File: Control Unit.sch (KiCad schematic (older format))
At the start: 54 parts, among them SW1 SW_Push-Switch, U19 7400, U20 74LS161-74xx, U21 AT28C64B-15PU, U22 AT28C64B-15PU, U23 AT28C64B-15PU

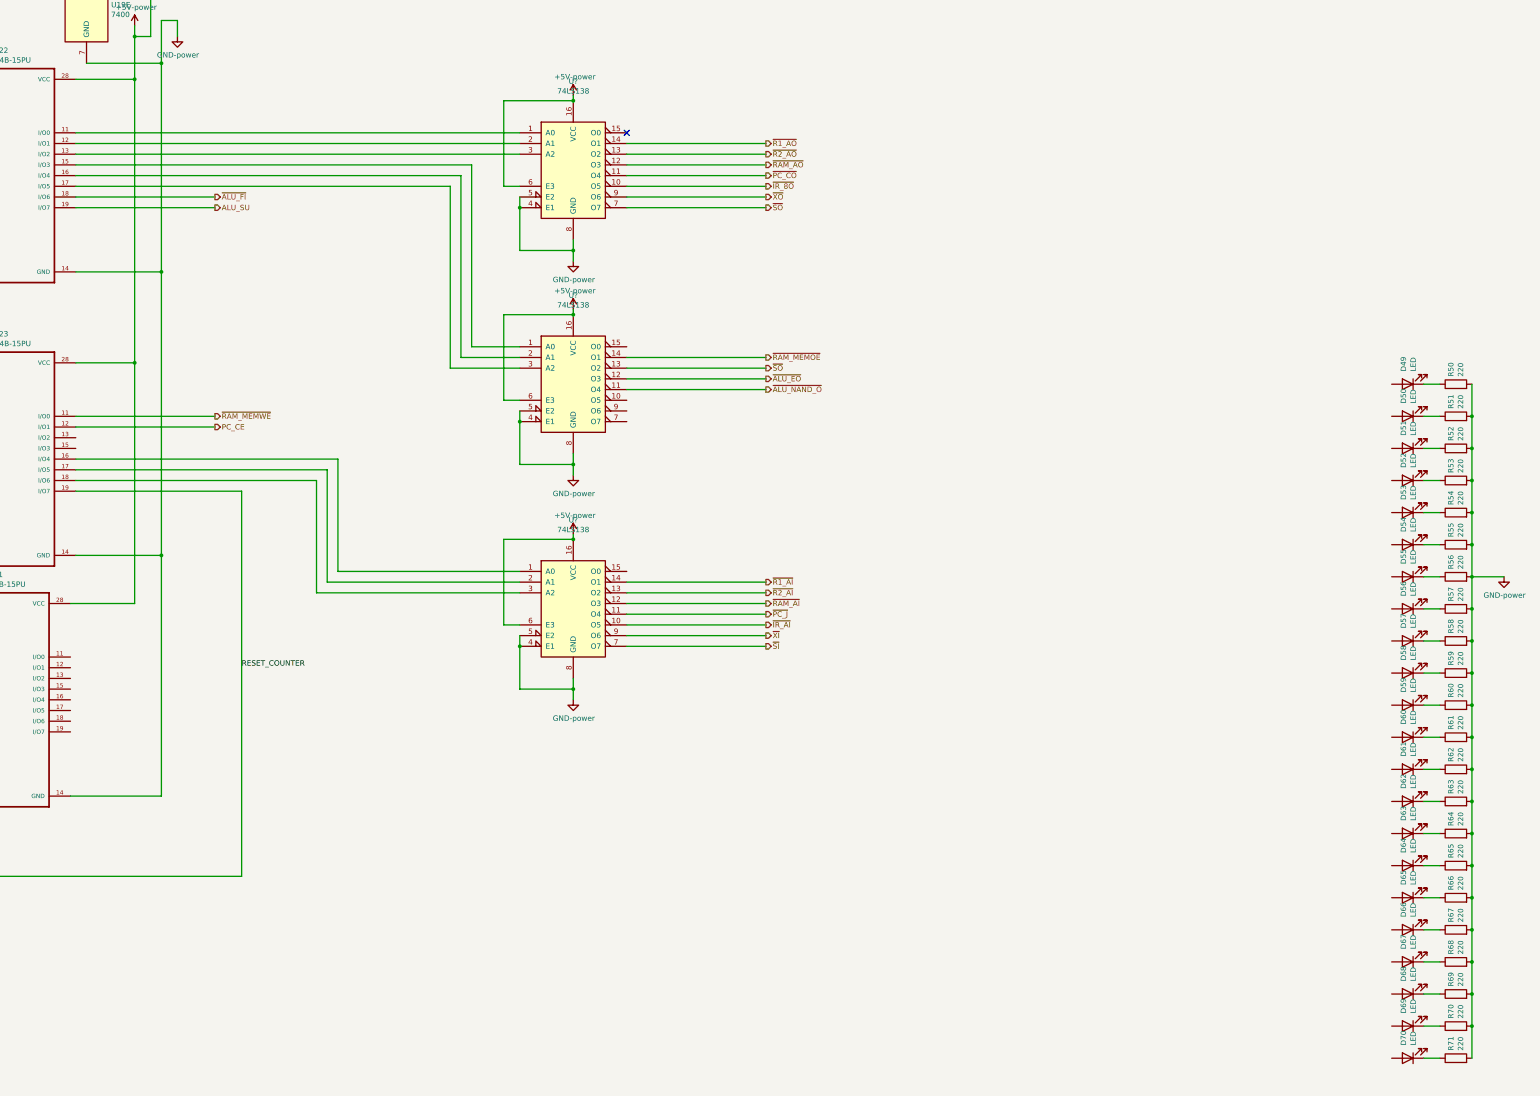
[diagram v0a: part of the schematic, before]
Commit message: using new RAM and ROM,15bits baby
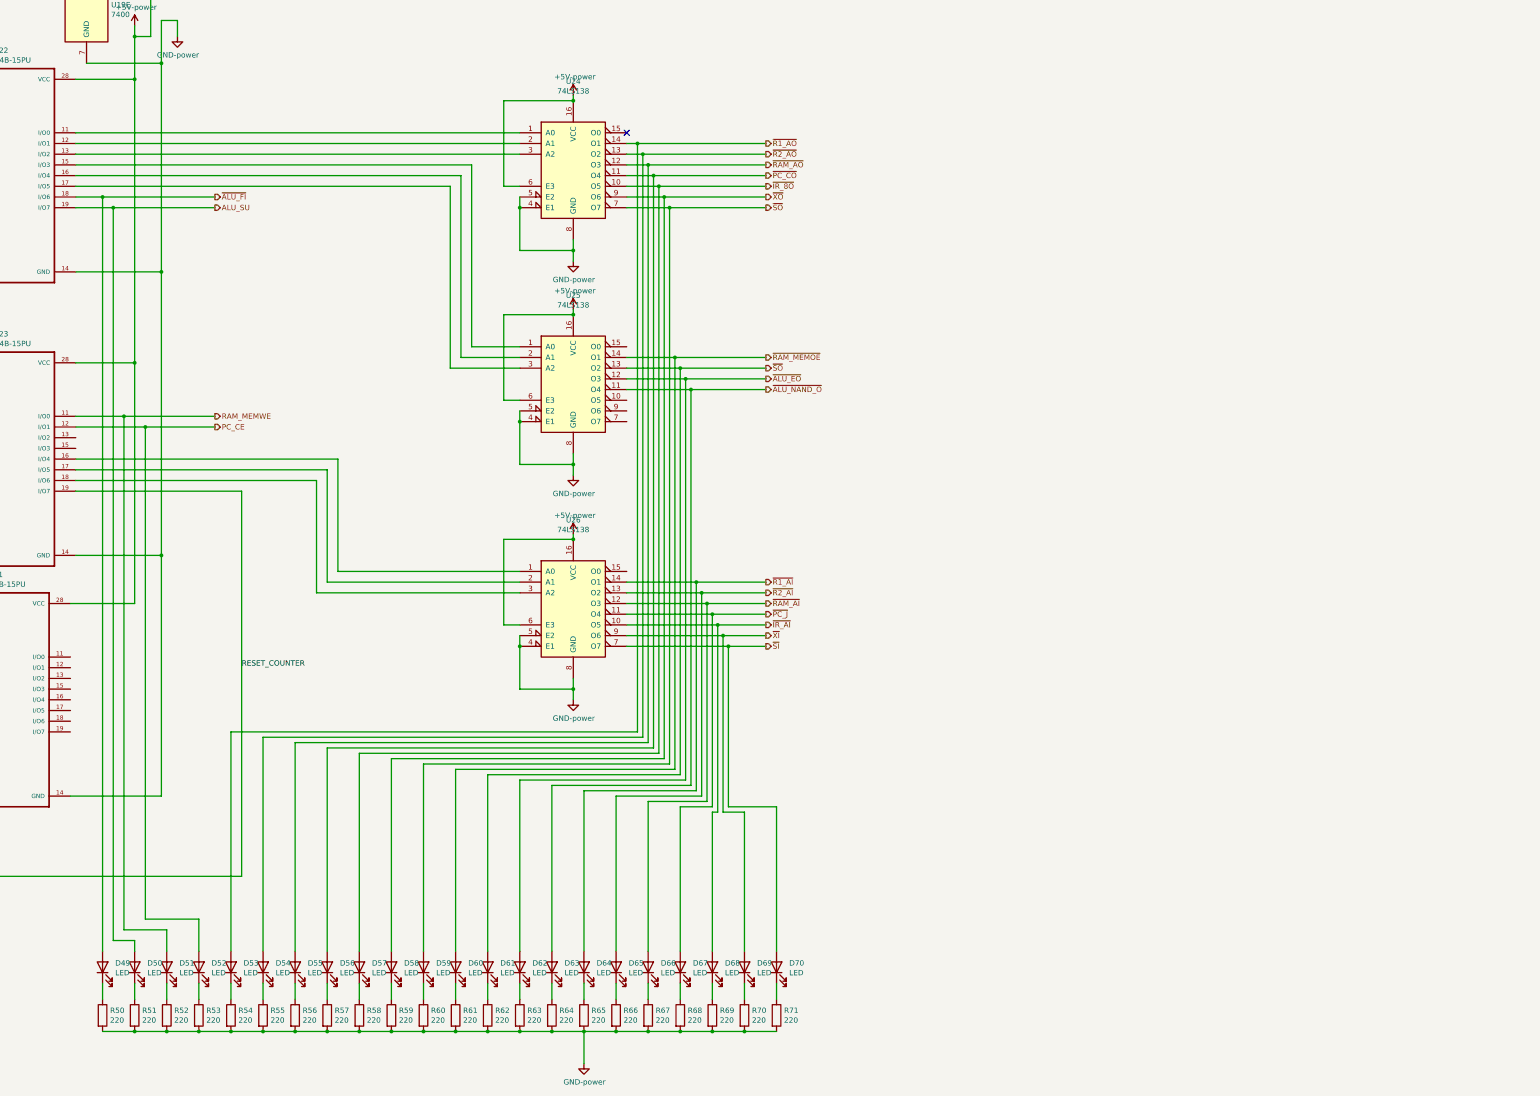
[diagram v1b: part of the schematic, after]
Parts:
- U24, U25, U26: renamed from U?; footprint (none) -> Package_DIP:DIP-16_W7.62mm
- renumbered D70 to D49, D69 to D50, D68 to D51, D67 to D52, D66 to D53, D65 to D54, D64 to D55, D63 to D56, D62 to D57, D61 to D58, D60 to D59, D59 to D60, D58 to D61, D57 to D62, D56 to D63, D55 to D64, D54 to D65, D53 to D66, D52 to D67, D51 to D68, D50 to D69, D49 to D70, R71 to R50, R70 to R51, R69 to R52, R68 to R53, R67 to R54, R66 to R55, R65 to R56, R64 to R57, R63 to R58, R62 to R59, R61 to R60, R60 to R61, R59 to R62, R58 to R63, R57 to R64, R56 to R65, R55 to R66, R54 to R67, R53 to R68, R52 to R69, R51 to R70, R50 to R71
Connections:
- net ~RAM_MEMWE is gone; now on net RAM_MEMWE: U23.11 (I/O0)
- net ALU_SU: now also D50.2 (A)
- net PC_CE: now also D52.2 (A)
- net ~ALU_EO: now also D62.2 (A)
- net ~ALU_FI: now also D49.2 (A)
- net ~ALU_NAND_O: now also D63.2 (A)
- net ~IR_8O: now also D57.2 (A)
- net ~IR_AI: now also D68.2 (A)
- net ~PC_CO: now also D56.2 (A)
- net ~PC_J: now also D67.2 (A)
- net ~R1_AI: now also D64.2 (A)
- net ~R1_AO: now also D53.2 (A)
- net ~R2_AI: now also D65.2 (A)
- net ~R2_AO: now also D54.2 (A)
- net ~RAM_AI: now also D66.2 (A)
- net ~RAM_AO: now also D55.2 (A)
- net ~RAM_MEMOE: now also D60.2 (A)
- net ~SI: now also D70.2 (A)
- net ~SO: now also D59.2 (A), D61.2 (A)
- net ~XI: now also D69.2 (A)
- net ~XO: now also D58.2 (A)
- net RAM_MEMWE: now reaches D51.2 (A)
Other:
- moved on the sheet: D49, D50, D51, D52, D53, D54, D55, D56, D57, D58, D59, D60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

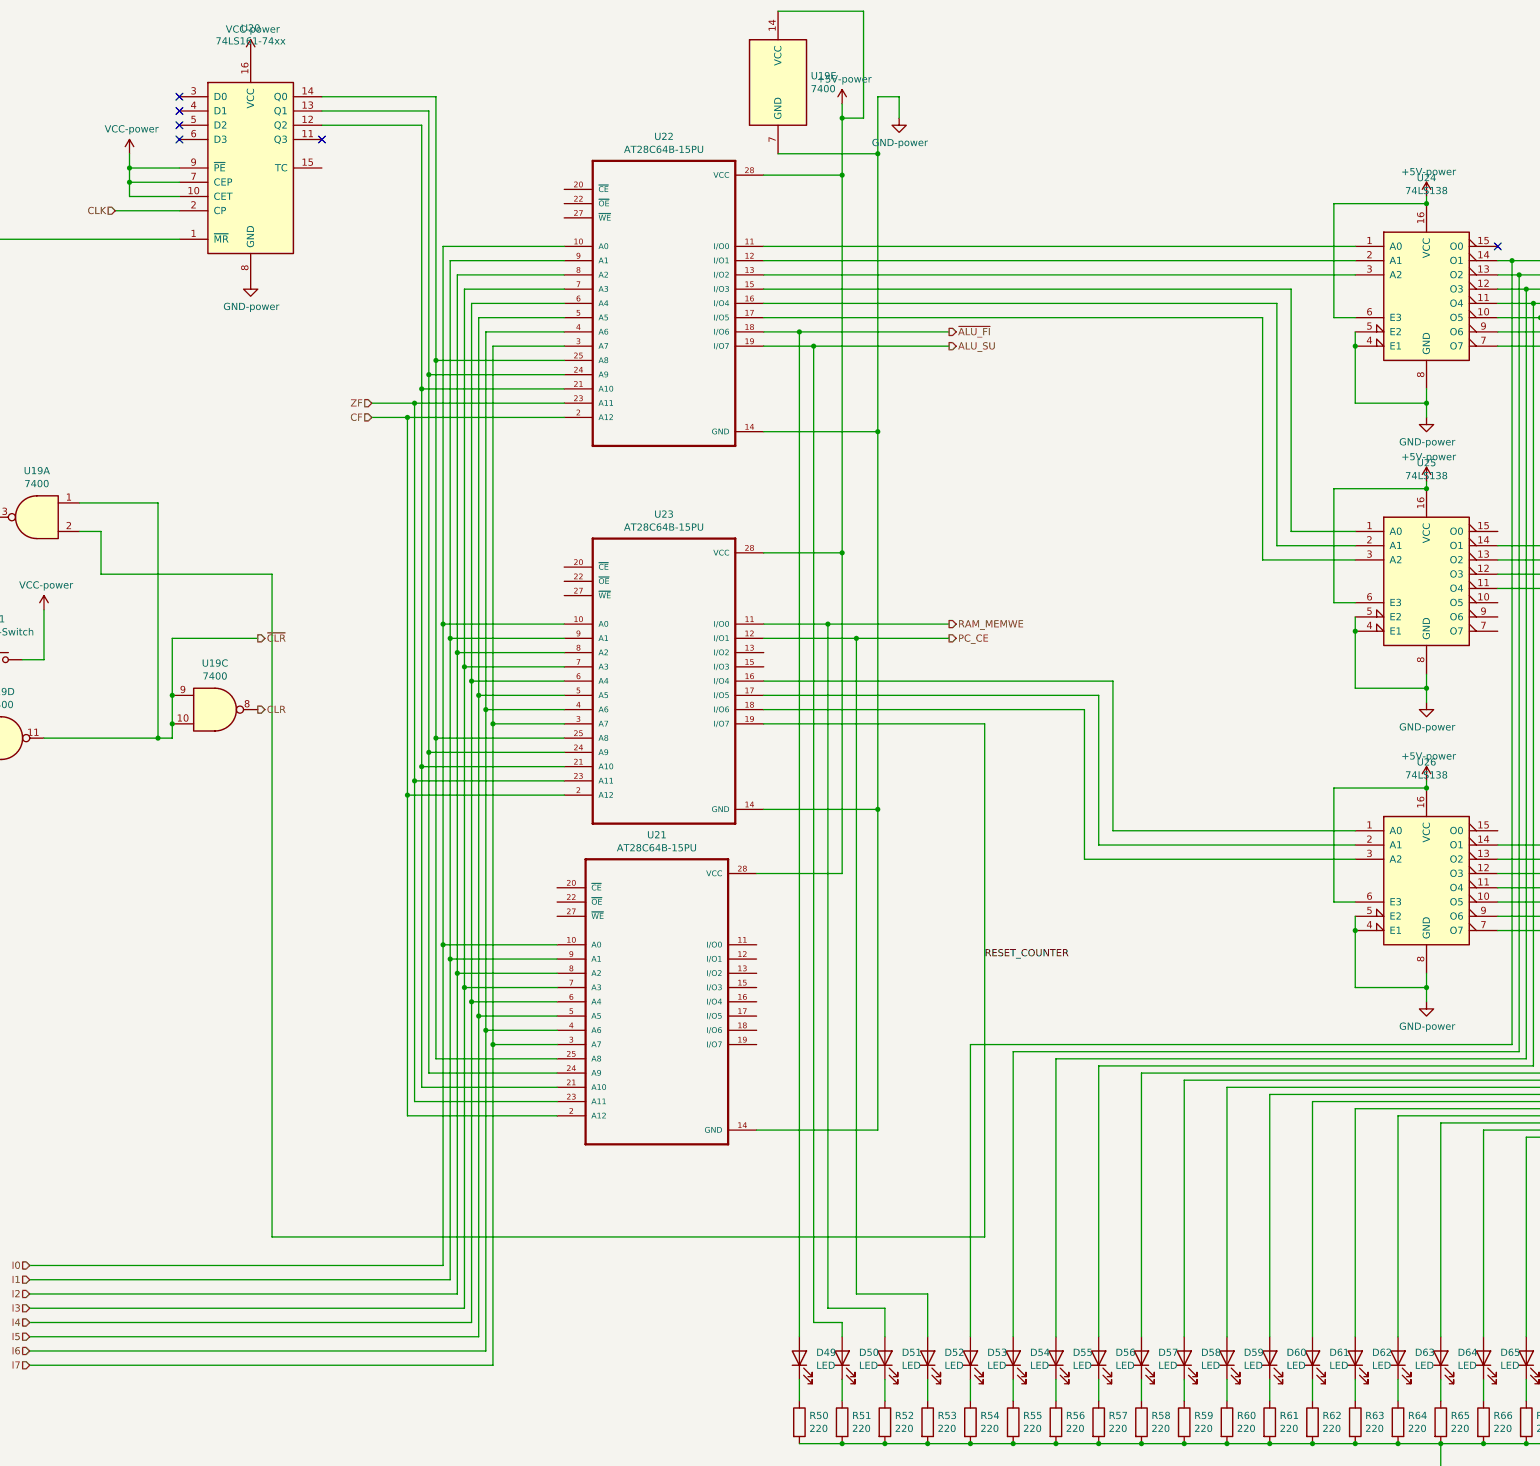
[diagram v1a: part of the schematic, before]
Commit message: using new ROM in CU and more jumps
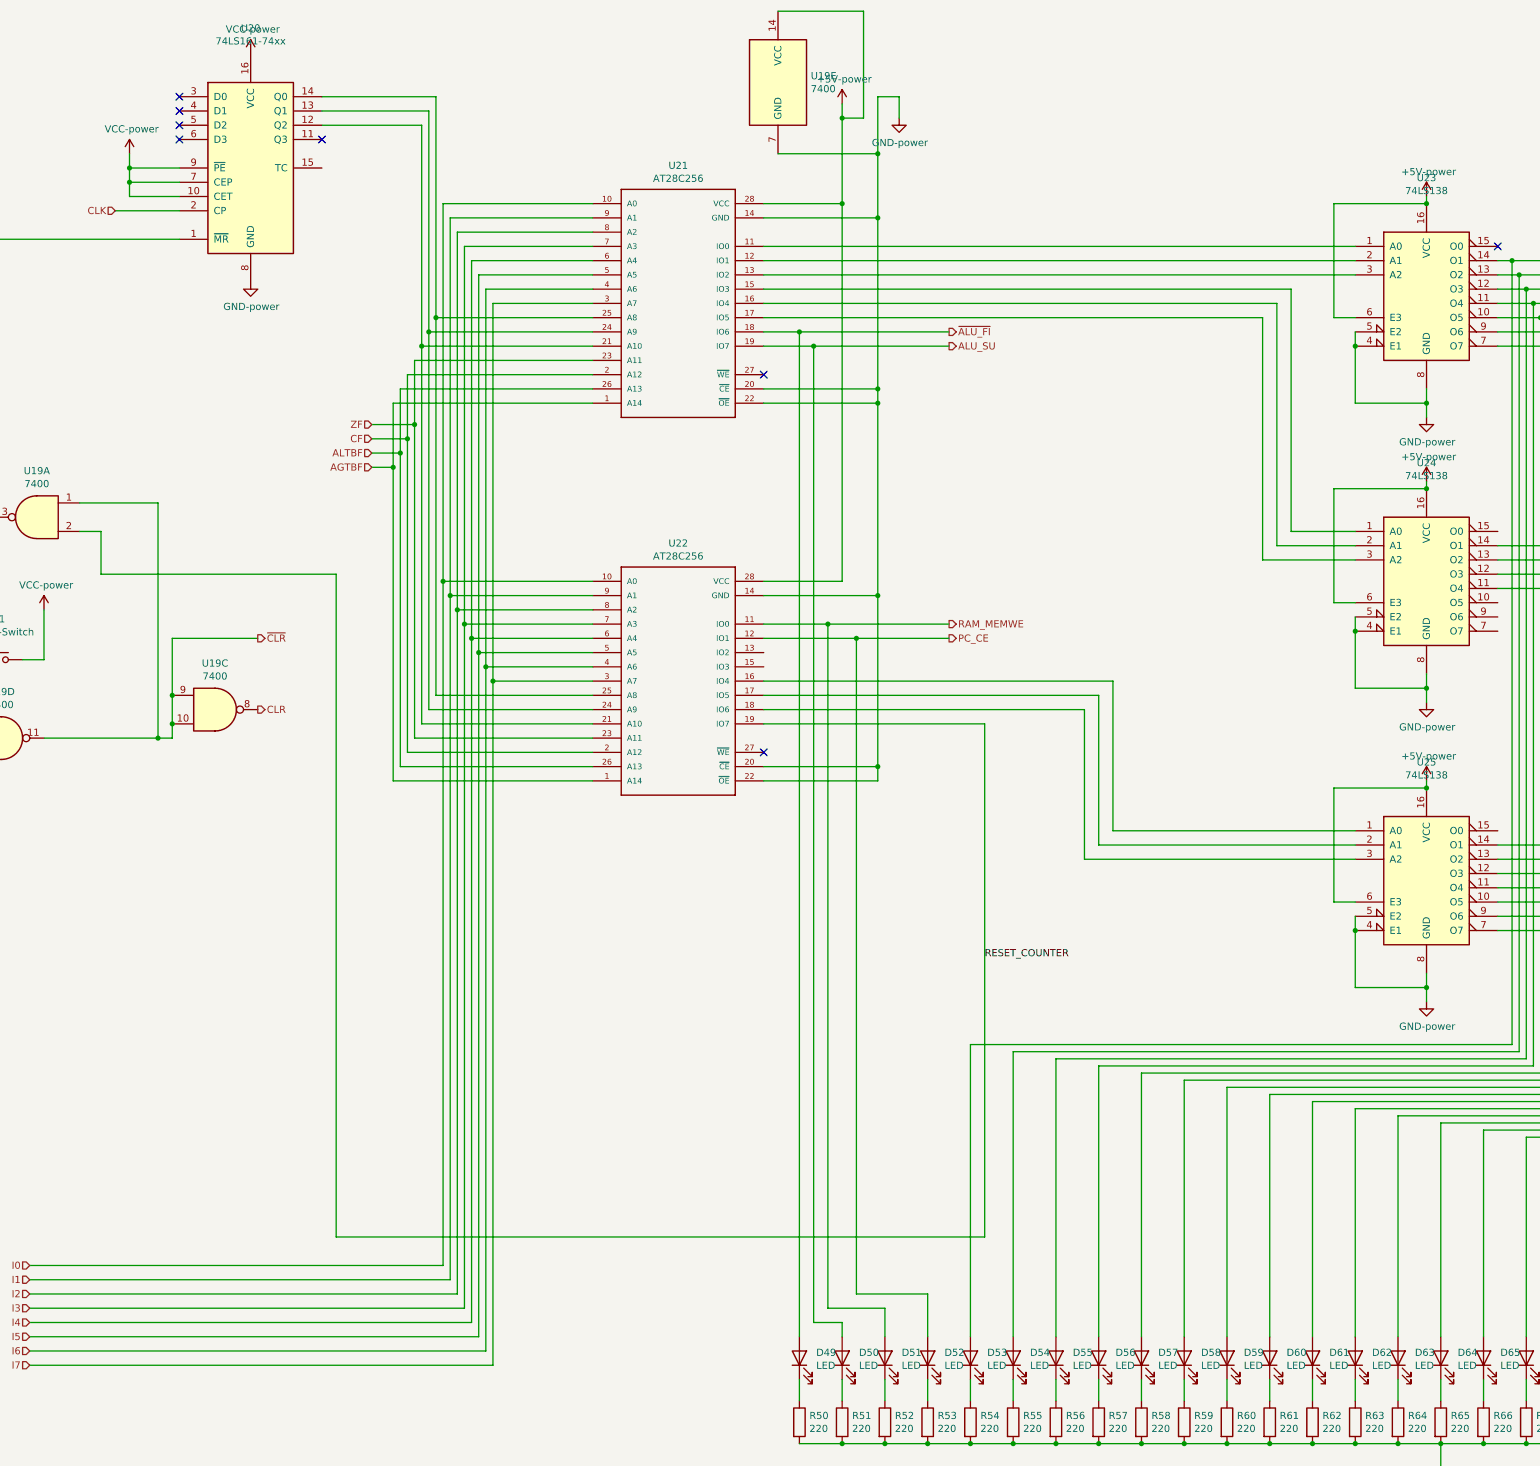
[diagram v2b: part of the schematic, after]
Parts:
- removed U21, U22, U23: AT28C64B-15PU, ROM:ZIF-AT28C64B-15PU, symbol AT28C64B-15PU:AT28C64B-15PU
- added U21, U22: AT28C256, ROM:ZIF-AT28C64B-15PU, symbol AT28C256:AT28C256
- renumbered U24 to U23, U25 to U24, U26 to U25
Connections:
- net +5V: now also U21.28 (VCC), U22.28 (VCC)
- net ALU_SU: now also U21.19 (IO7)
- net CF: now also U21.2 (A12), U22.2 (A12)
- net GND: now also U21.14 (GND), U21.20 (~CE~), U21.22 (~OE~), U22.14 (GND), U22.20 (~CE~), U22.22 (~OE~)
- net I0: now also U21.10 (A0), U22.10 (A0)
- net I1: now also U21.9 (A1), U22.9 (A1)
- net I2: now also U21.8 (A2), U22.8 (A2)
- net I3: now also U21.7 (A3), U22.7 (A3)
- net I4: now also U21.6 (A4), U22.6 (A4)
- net I5: now also U21.5 (A5), U22.5 (A5)
- net I6: now also U21.4 (A6), U22.4 (A6)
- net I7: now also U21.3 (A7), U22.3 (A7)
- net PC_CE: now also U22.12 (IO1)
- net RAM_MEMWE: now also U22.11 (IO0)
- net RESET_COUNTER: now also U22.19 (IO7)
- net ZF: now also U21.23 (A11), U22.23 (A11)
- net ~ALU_FI: now also U21.18 (IO6)
- net at U20.12 (Q2): now also U21.21 (A10), U22.21 (A10)
- net at U20.13 (Q1): now also U21.24 (A9), U22.24 (A9)
- net at U20.14 (Q0): now also U21.25 (A8), U22.25 (A8)
- net at U23.1 (A0): now also U21.11 (IO0)
- net at U23.2 (A1): now also U21.12 (IO1)
- net at U23.3 (A2): now also U21.13 (IO2)
- net at U24.1 (A0): now also U21.15 (IO3)
- net at U24.2 (A1): now also U21.16 (IO4)
- net at U24.3 (A2): now also U21.17 (IO5)
- net at U25.1 (A0): now also U22.16 (IO4)
- net at U25.2 (A1): now also U22.17 (IO5)
- net at U25.3 (A2): now also U22.18 (IO6)
- new net AGTBF: U21.1 (A14), U22.1 (A14)
- new net ALTBF: U21.26 (A13), U22.26 (A13)
- no-connect marks 6 -> 8
